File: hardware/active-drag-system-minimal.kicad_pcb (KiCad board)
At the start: 4 copper layers, 33 x 81.8 mm, 86 parts, among them J1 Conn_01x02_Pin, J2 Conn_01x02_Socket, J3 10118193-0001LF, J4 Conn_01x10, J5 Conn_01x02_Pin, J6 Conn_01x02_Pin, J8 Conn_01x03_Pin, SW1 PTS815 SJM 250 SMTR LFS, U1 RP2040, U2 W25Q128JVSIQ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

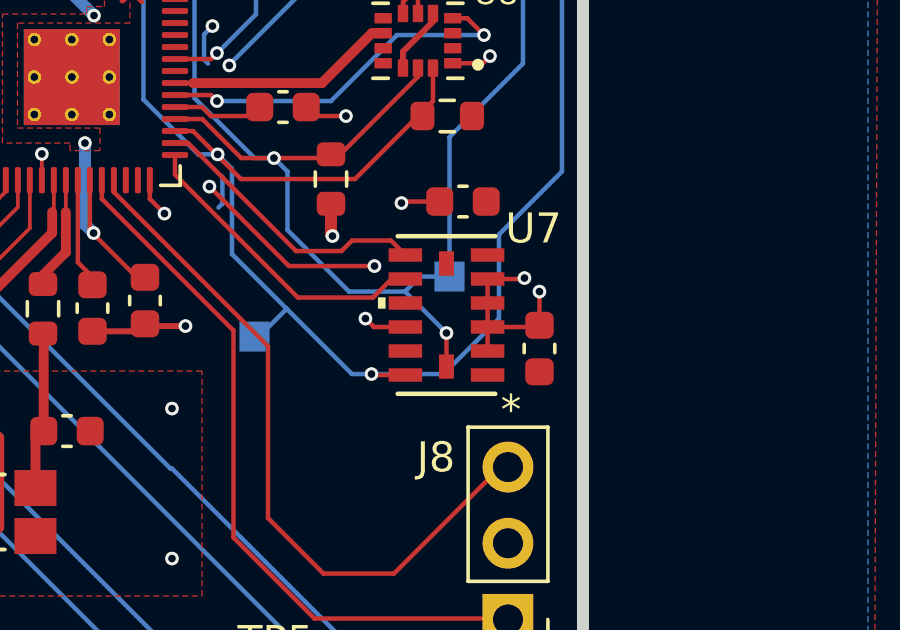
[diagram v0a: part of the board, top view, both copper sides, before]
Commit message: Removed bad GND connection to reserved pin on ADXL375 IMU; first error found in first batch
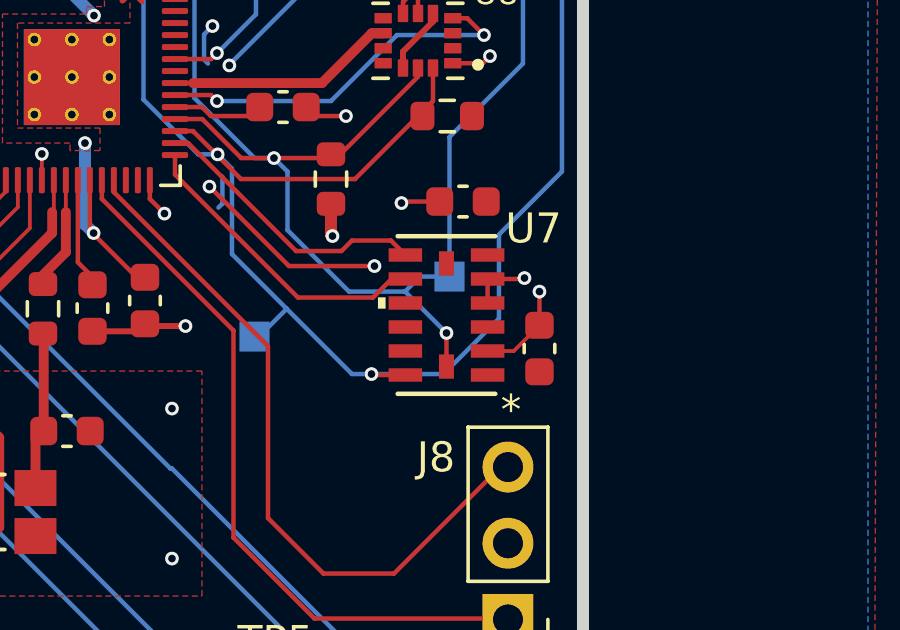
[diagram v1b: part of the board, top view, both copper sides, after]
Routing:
- net GND: track 199.5 -> 196.8 mm, vias 64 -> 63
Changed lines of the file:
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@@
+	)
+	(segment
+		(start 161.320901 96.131502)
+		(end 162.193498 96.131502)
+		(width 0.127)
+		(layer "F.Cu")
+		(net 1)
 	)
 	(segment
@@
 	)
 	(segment
-		(start 157.531501 95.331501)
-		(end 157.25 95.05)
-		(width 0.15)
-		(layer "F.Cu")
-		(net 1)
-	)
-	(segment
 		(start 149.65 95.475)
 		(end 149.9 95.225)
@@
 	)
 	(segment
-		(start 161.320901 96.131502)
-		(end 161.320901 93.731502)
-		(width 0.15)
-		(layer "F.Cu")
-		(net 1)
-	)
-	(segment
 		(start 137.05 95.65)
 		(end 139.55 93.15)
@@
 	)
 	(segment
+		(start 161.320901 93.731502)
+		(end 161.320901 94.531503)
+		(width 0.15)
+		(layer "F.Cu")
+		(net 1)
+	)
+	(segment
 		(start 149.975 95.3)
 		(end 149.9 95.225)
@@
 	)
 	(segment
+		(start 162.193498 96.131502)
+		(end 163.05 95.275)
+		(width 0.127)
+		(layer "F.Cu")
+		(net 1)
+	)
+	(segment
 		(start 141.550001 71.674999)
 		(end 137.049999 71.674999)
@@
 	)
 	(segment
-		(start 161.320901 95.331501)
-		(end 162.993499 95.331501)
-		(width 0.15)
-		(layer "F.Cu")
-		(net 1)
-	)
-	(segment
 		(start 158.8 83.775)
 		(end 159.775 82.8)
@@
 	)
 	(segment
-		(start 158.579099 95.331501)
-		(end 157.531501 95.331501)
-		(width 0.15)
-		(layer "F.Cu")
-		(net 1)
-	)
-	(segment
 		(start 151.65 62.2)
 		(end 151.75 62.1)
@@
 		(size 0.4572)
 		(drill 0.254)
-		(layers "F.Cu" "B.Cu")
-		(free yes)
-		(net 1)
-	)
-	(via
-		(at 157.25 95.05)
-		(size 0.4572)
-		(drill 0.254)
